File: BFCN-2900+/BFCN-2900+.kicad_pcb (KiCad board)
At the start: 2 copper layers, 60 x 30 mm, 138 parts, among them U1 BFCN-2900+, X1 SMA-F, X2 SMA-F

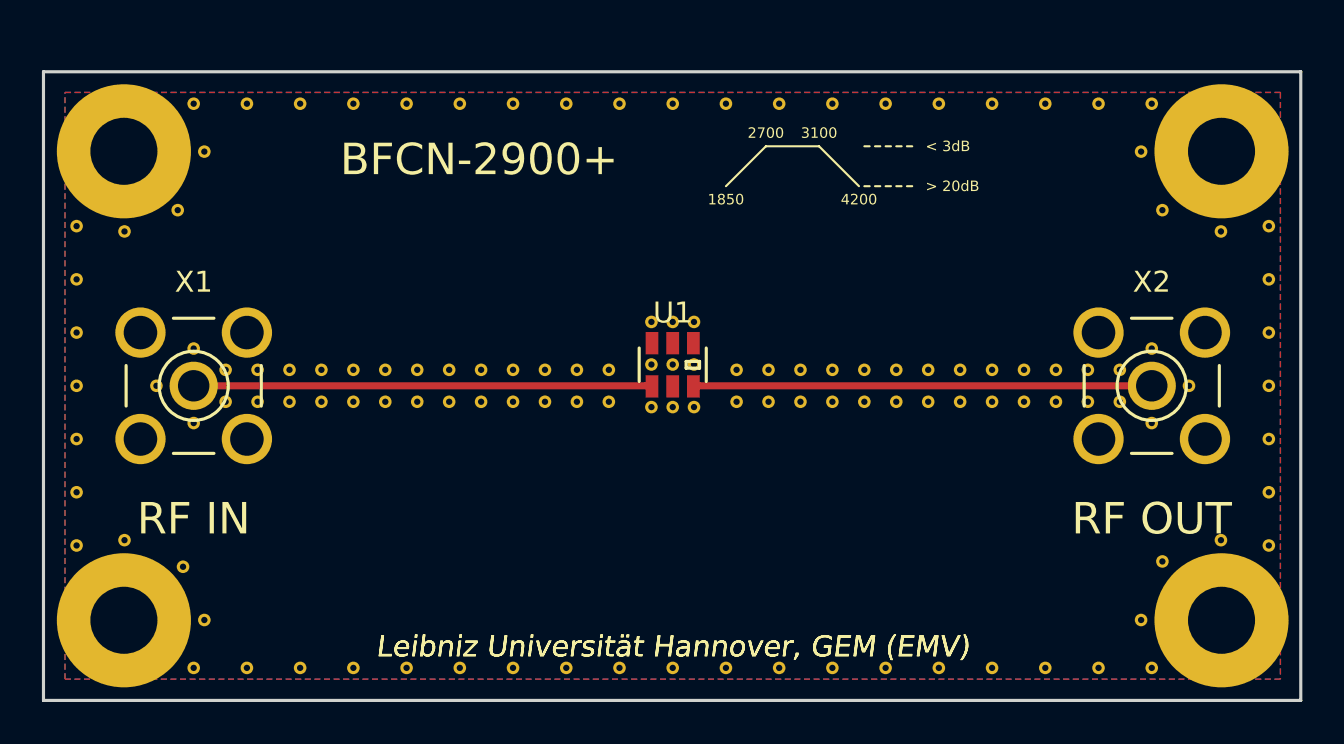
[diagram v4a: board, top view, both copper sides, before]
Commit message: BFCN-2900+: corrected 50Ohm CPW, new VIA arrangement
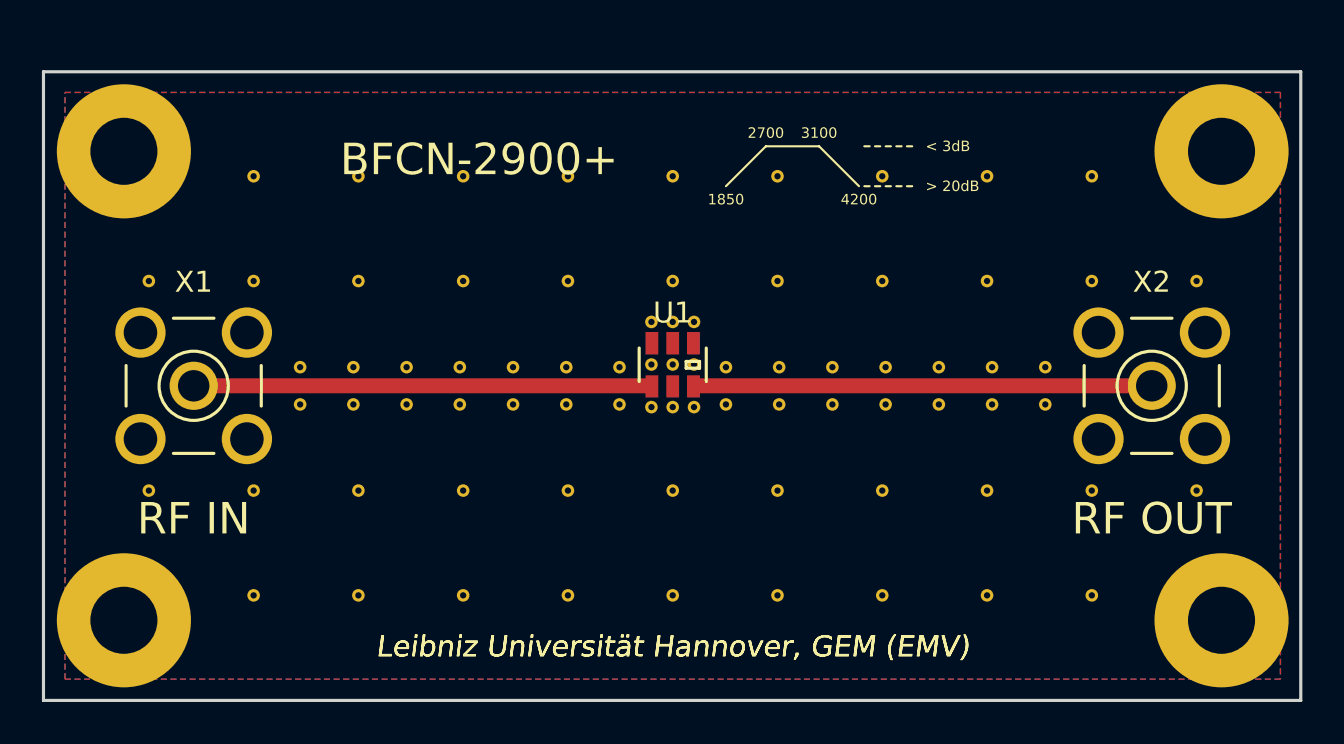
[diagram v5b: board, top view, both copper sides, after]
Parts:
- removed the REF** at (97.2, 106.8)
- removed the REF** at (95.4, 105.0)
- removed the REF** at (97.2, 103.2)
- removed the REF** at (98.7, 104.2)
- removed REF**101 (x4), REF**1101 (x2), REF**111 (x2), REF**1112 (x2), REF**1113 (x2), REF**1114 (x2), REF**1115 (x2), REF**1116 (x2), REF**1117 (x2), REF**1181 (x2), REF**1191 (x8), REF**121 (x2), REF**131 (x2), REF**141 (x2), REF**151 (x2), REF**161 (x2), REF**171 (x2), REF**181 (x2), REF**191 (x2), REF**21 (x6), REF**31 (x4), REF**41 (x4), REF**51 (x4), REF**61 (x4), REF**71 (x4), REF**81 (x4), REF**91 (x4): VIA-0.3, JueVias:VIA-0.3
- removed the REF**11 at (123.1, 105.7)
- removed the REF**11 at (142.9, 103.2)
- removed the REF**11 at (139.8, 105.7)
- removed the REF**11 at (141.4, 105.7)
- removed the REF**11 at (141.4, 104.2)
- removed the REF**11 at (139.8, 104.2)
- removed the REF**11 at (115.5, 104.2)
- removed the REF**11 at (113.9, 104.2)
- removed the REF**11 at (115.5, 105.7)
- removed the REF**11 at (113.9, 105.7)
- removed the REF**11 at (98.7, 105.7)
- removed the REF**11 at (117.0, 105.7)
- removed the REF**11 at (117.0, 104.2)
- removed the REF**11 at (142.9, 106.8)
- removed the REF**11 at (144.7, 105.0)
- removed the REF**1111 at (96.7, 113.6)
- removed the REF**1111 at (122.6, 91.5)
- removed the REF**1111 at (97.7, 116.2)
- removed the REF**1111 at (93.9, 112.4)
- removed the REF**1111 at (93.9, 97.6)
- removed the REF**1111 at (96.4, 96.6)
- removed the REF**1111 at (97.7, 93.8)
- removed the REF**1111 at (148.5, 97.4)
- removed the REF**1111 at (91.6, 97.4)
- removed the REF**1111 at (122.6, 118.4)
- removed the REF**1121 at (125.1, 118.4)
- removed the REF**1121 at (125.1, 91.5)
- removed the REF**1131 at (127.6, 118.4)
- removed the REF**1131 at (127.6, 91.5)
- removed the REF**1141 at (130.2, 118.4)
- removed the REF**1141 at (130.2, 91.5)
- removed the REF**1151 at (132.7, 118.4)
- removed the REF**1151 at (132.7, 91.5)
- removed the REF**1161 at (135.3, 118.4)
- removed the REF**1161 at (135.3, 91.5)
- removed the REF**1171 at (137.8, 118.4)
- removed the REF**1171 at (137.8, 91.5)
- added REF**1111: VIA-0.3, JueVias:VIA-0.3, F.Cu at (102.2, 104.1)
- added REF**11111: VIA-0.3, JueVias:VIA-0.3, F.Cu at (102.2, 105.9)
- added REF**11111: VIA-0.3, JueVias:VIA-0.3, F.Cu at (122.6, 105.9)
- added REF**11121: VIA-0.3, JueVias:VIA-0.3, F.Cu at (104.8, 105.9)
- added REF**11121: VIA-0.3, JueVias:VIA-0.3, F.Cu at (125.1, 105.9)
- added REF**11131: VIA-0.3, JueVias:VIA-0.3, F.Cu at (107.3, 105.9)
- added REF**11131: VIA-0.3, JueVias:VIA-0.3, F.Cu at (127.6, 105.9)
- added REF**11141: VIA-0.3, JueVias:VIA-0.3, F.Cu at (109.9, 105.9)
- added REF**11141: VIA-0.3, JueVias:VIA-0.3, F.Cu at (130.2, 105.9)
- added REF**11151: VIA-0.3, JueVias:VIA-0.3, F.Cu at (112.4, 105.9)
- added REF**11151: VIA-0.3, JueVias:VIA-0.3, F.Cu at (132.7, 105.9)
- added REF**11161: VIA-0.3, JueVias:VIA-0.3, F.Cu at (114.9, 105.9)
- added REF**11161: VIA-0.3, JueVias:VIA-0.3, F.Cu at (135.3, 105.9)
- added REF**11171: VIA-0.3, JueVias:VIA-0.3, F.Cu at (117.5, 105.9)
- added REF**11171: VIA-0.3, JueVias:VIA-0.3, F.Cu at (137.8, 105.9)
- added REF**1121: VIA-0.3, JueVias:VIA-0.3, F.Cu at (104.8, 104.1)
- added REF**1121: VIA-0.3, JueVias:VIA-0.3, F.Cu at (125.1, 104.1)
- added REF**1131: VIA-0.3, JueVias:VIA-0.3, F.Cu at (107.3, 104.1)
- added REF**1131: VIA-0.3, JueVias:VIA-0.3, F.Cu at (127.6, 104.1)
- added REF**1141: VIA-0.3, JueVias:VIA-0.3, F.Cu at (109.9, 104.1)
- added REF**1141: VIA-0.3, JueVias:VIA-0.3, F.Cu at (130.2, 104.1)
- added REF**1151: VIA-0.3, JueVias:VIA-0.3, F.Cu at (112.4, 104.1)
- added REF**1151: VIA-0.3, JueVias:VIA-0.3, F.Cu at (132.7, 104.1)
- added REF**1161: VIA-0.3, JueVias:VIA-0.3, F.Cu at (114.9, 104.1)
- added REF**1161: VIA-0.3, JueVias:VIA-0.3, F.Cu at (135.3, 104.1)
- added REF**1171: VIA-0.3, JueVias:VIA-0.3, F.Cu at (117.5, 104.1)
- added REF**1171: VIA-0.3, JueVias:VIA-0.3, F.Cu at (137.8, 104.1)
- added REF**11711102: VIA-0.3, JueVias:VIA-0.3, F.Cu at (135.0, 95.0)
- added REF**11711103: VIA-0.3, JueVias:VIA-0.3, F.Cu at (135.0, 100.0)
- added REF**11711105: VIA-0.3, JueVias:VIA-0.3, F.Cu at (135.0, 110.0)
- added REF**11711106: VIA-0.3, JueVias:VIA-0.3, F.Cu at (135.0, 115.0)
- added REF**11711112: VIA-0.3, JueVias:VIA-0.3, F.Cu at (140.0, 95.0)
- added REF**11711113: VIA-0.3, JueVias:VIA-0.3, F.Cu at (140.0, 100.0)
- added REF**11711115: VIA-0.3, JueVias:VIA-0.3, F.Cu at (140.0, 110.0)
- added REF**11711116: VIA-0.3, JueVias:VIA-0.3, F.Cu at (140.0, 115.0)
- added REF**11711123: VIA-0.3, JueVias:VIA-0.3, F.Cu at (145.0, 100.0)
- added REF**11711125: VIA-0.3, JueVias:VIA-0.3, F.Cu at (145.0, 110.0)
- added REF**1171123: VIA-0.3, JueVias:VIA-0.3, F.Cu at (95.0, 100.0)
- added REF**1171125: VIA-0.3, JueVias:VIA-0.3, F.Cu at (95.0, 110.0)
- added REF**1171132: VIA-0.3, JueVias:VIA-0.3, F.Cu at (100.0, 95.0)
- added REF**1171133: VIA-0.3, JueVias:VIA-0.3, F.Cu at (100.0, 100.0)
- added REF**1171135: VIA-0.3, JueVias:VIA-0.3, F.Cu at (100.0, 110.0)
- added REF**1171136: VIA-0.3, JueVias:VIA-0.3, F.Cu at (100.0, 115.0)
- added REF**1171142: VIA-0.3, JueVias:VIA-0.3, F.Cu at (105.0, 95.0)
- added REF**1171143: VIA-0.3, JueVias:VIA-0.3, F.Cu at (105.0, 100.0)
- added REF**1171145: VIA-0.3, JueVias:VIA-0.3, F.Cu at (105.0, 110.0)
- added REF**1171146: VIA-0.3, JueVias:VIA-0.3, F.Cu at (105.0, 115.0)
- added REF**1171152: VIA-0.3, JueVias:VIA-0.3, F.Cu at (110.0, 95.0)
- added REF**1171153: VIA-0.3, JueVias:VIA-0.3, F.Cu at (110.0, 100.0)
- added REF**1171155: VIA-0.3, JueVias:VIA-0.3, F.Cu at (110.0, 110.0)
- added REF**1171156: VIA-0.3, JueVias:VIA-0.3, F.Cu at (110.0, 115.0)
- added REF**1171162: VIA-0.3, JueVias:VIA-0.3, F.Cu at (115.0, 95.0)
- added REF**1171163: VIA-0.3, JueVias:VIA-0.3, F.Cu at (115.0, 100.0)
- added REF**1171165: VIA-0.3, JueVias:VIA-0.3, F.Cu at (115.0, 110.0)
- added REF**1171166: VIA-0.3, JueVias:VIA-0.3, F.Cu at (115.0, 115.0)
- added REF**1171172: VIA-0.3, JueVias:VIA-0.3, F.Cu at (120.0, 95.0)
- added REF**1171173: VIA-0.3, JueVias:VIA-0.3, F.Cu at (120.0, 100.0)
- added REF**1171175: VIA-0.3, JueVias:VIA-0.3, F.Cu at (120.0, 110.0)
- added REF**1171176: VIA-0.3, JueVias:VIA-0.3, F.Cu at (120.0, 115.0)
- added REF**1171182: VIA-0.3, JueVias:VIA-0.3, F.Cu at (125.0, 95.0)
- added REF**1171183: VIA-0.3, JueVias:VIA-0.3, F.Cu at (125.0, 100.0)
- added REF**1171185: VIA-0.3, JueVias:VIA-0.3, F.Cu at (125.0, 110.0)
- added REF**1171186: VIA-0.3, JueVias:VIA-0.3, F.Cu at (125.0, 115.0)
- added REF**1171192: VIA-0.3, JueVias:VIA-0.3, F.Cu at (130.0, 95.0)
- added REF**1171193: VIA-0.3, JueVias:VIA-0.3, F.Cu at (130.0, 100.0)
- added REF**1171195: VIA-0.3, JueVias:VIA-0.3, F.Cu at (130.0, 110.0)
- added REF**1171196: VIA-0.3, JueVias:VIA-0.3, F.Cu at (130.0, 115.0)
- moved REF**1111 0.52 mm to (122.6, 104.1)
- turned REF** to 90 degrees
- renumbered REF**11 to REF**1111
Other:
- net class 50Ohm: clearance 0.2 -> 0.15; trace_width 0.336 -> 0.714
- net class Default: clearance 0.1 -> 0.15
- rule trace_clearance: 0.1 -> 0.15
